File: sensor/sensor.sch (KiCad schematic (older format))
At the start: 42 parts, among them J1 5V, J2 CAN IN, J3 CAN OUT, J4 AVR-ISP-6, J5 SENSOR IN, J6 SENSOR VCC, J7 SENSOR GND, U1 ATmega32M1-AU, U2 MCP2551-I-SN, Y1 16MHz

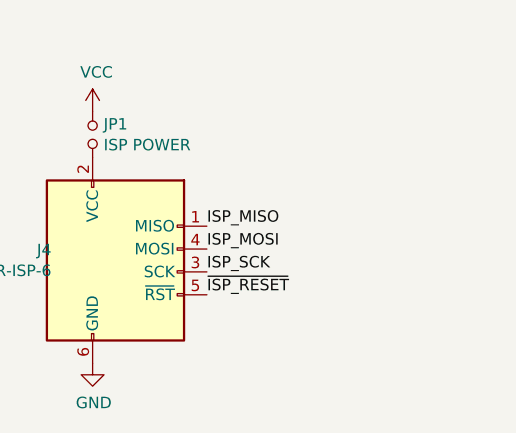
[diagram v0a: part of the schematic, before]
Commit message: Added power LED to sensor board
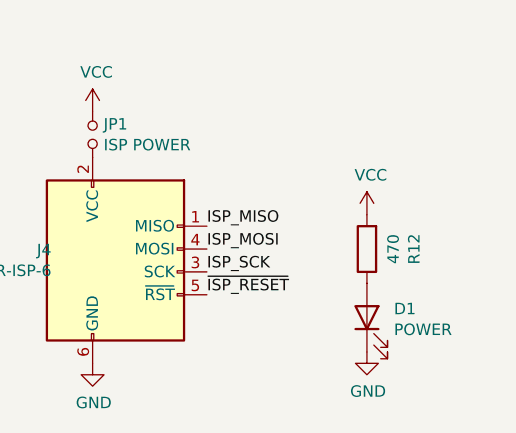
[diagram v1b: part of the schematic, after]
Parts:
- added D1: POWER, LED_SMD:LED_0805_2012Metric_Pad1.15x1.40mm_HandSolder, symbol Device:LED
- added R12: 470, Resistor_SMD:R_0805_2012Metric_Pad1.15x1.40mm_HandSolder, symbol Device:R
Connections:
- net GND: now also D1.1 (K)
- net VCC: now also R12.2
- new net: D1.2 (A), R12.1
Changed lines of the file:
@@
 Wire Wire Line
 	10250 3350 10250 3250
+$Comp
+L Device:LED D1
+U 1 1 5CB27B95
+P 10600 5500
+F 0 "D1" V 10638 5382 50  0000 R CNN
+F 1 "POWER" V 10547 5382 50  0000 R CNN
+F 2 "LED_SMD:LED_0805_2012Metric_Pad1.15x1.40mm_HandSolder" H 10600 5500 50  0001 C CNN
+F 3 "~" H 10600 5500 50  0001 C CNN
+	1    10600 5500
+	0    -1   -1   0
+$EndComp
+$Comp
+L Device:R R12
+U 1 1 5CB27E55
+P 10600 5200
+F 0 "R12" V 10393 5200 50  0000 C CNN
+F 1 "470" V 10484 5200 50  0000 C CNN
+F 2 "Resistor_SMD:R_0805_2012Metric_Pad1.15x1.40mm_HandSolder" V 10530 5200 50  0001 C CNN
+F 3 "~" H 10600 5200 50  0001 C CNN
+	1    10600 5200
+	-1   0    0    1
+$EndComp
+$Comp
+L power:VCC #PWR0105
+U 1 1 5CB27F09
+P 10600 5050
+F 0 "#PWR0105" H 10600 4900 50  0001 C CNN
+F 1 "VCC" H 10617 5223 50  0000 C CNN
+F 2 "" H 10600 5050 50  0001 C CNN
+F 3 "" H 10600 5050 50  0001 C CNN
+	1    10600 5050
+	1    0    0    -1
+$EndComp
+$Comp
+L power:GND #PWR0106
+U 1 1 5CB27FF0
+P 10600 5650
+F 0 "#PWR0106" H 10600 5400 50  0001 C CNN
+F 1 "GND" H 10605 5477 50  0000 C CNN
+F 2 "" H 10600 5650 50  0001 C CNN
+F 3 "" H 10600 5650 50  0001 C CNN
+	1    10600 5650
+	1    0    0    -1
+$EndComp
 $EndSCHEMATC

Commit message: sensor: modernize
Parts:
- removed J2: CAN IN, TerminalBlock_TE-Connectivity:TerminalBlock_TE_282834-2_1x02_P2.54mm_Horizontal, symbol Connector_Generic:Conn_01x02
- removed J3: CAN OUT, TerminalBlock_TE-Connectivity:TerminalBlock_TE_282834-2_1x02_P2.54mm_Horizontal, symbol Connector_Generic:Conn_01x02
- added C18: 100n, Capacitor_SMD:C_0805_2012Metric_Pad1.15x1.40mm_HandSolder, symbol Device:C
- added H3: SW, MountingHole:MountingHole_3.2mm_M3_Pad, symbol Mechanical:MountingHole_Pad
- added H4: SE, MountingHole:MountingHole_3.2mm_M3_Pad, symbol Mechanical:MountingHole_Pad
- added J2: CAN, TerminalBlock_TE-Connectivity:TerminalBlock_TE_282834-6_1x06_P2.54mm_Horizontal, symbol Connector_Generic:Conn_01x06
- added R13: DNP/0, Resistor_SMD:R_0805_2012Metric_Pad1.15x1.40mm_HandSolder, symbol Device:R
- added U3: LM2937xMP, Package_TO_SOT_SMD:SOT-223-3_TabPin2, symbol Regulator_Linear:LM2937xMP
- C3: footprint Capacitor_THT:CP_Radial_D5.0mm_P2.00mm -> Capacitor_SMD:C_0805_2012Metric_Pad1.15x1.40mm_HandSolder; symbol Device:CP -> Device:C
- J1: value 5V -> 12V
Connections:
- net CAN_N: now also J2.2 (Pin_2), J2.5 (Pin_5)
- net CAN_P: now also J2.3 (Pin_3), J2.4 (Pin_4)
- net GND: now also C18.2, H3.1, H4.1, J2.1 (Pin_1), J2.6 (Pin_6), U3.2 (GND)
- net VCC: now also R13.1, U3.3 (VO); no longer J1.2 (Pin_2)
- new net: C18.1, J1.2 (Pin_2), R13.2, U3.1 (VI)
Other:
- moved on the sheet: C1, C10, C15, C2, C4, C9, J1, L1, U1, Y1
